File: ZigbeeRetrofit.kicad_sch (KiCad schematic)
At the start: 23 parts, among them J1 110990030, J2 U.FL-R-SMT-1(10), J3 TC2050-IDC-NL, U1 CC2531F256RHAT, U2 SPX3819M5-L-3-3, Y1 32 Mhz, Y2 32.768 khz

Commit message: Updated crystals
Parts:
- removed Y2: 32.768 khz, symbol Device:Crystal
- added Y2: ECS-.327-12.5-34RR-TR, ECS-.327-12:XTAL_ECS-.327-12.5-34RR-TR, symbol ECS-.327-12.5-34RR-TR:ECS-.327-12.5-34RR-TR
- Y1: footprint XTAL_ECS-320-13-42-CKM-TR -> ECS-320-13-42-CKM-TR:XTAL_ECS-320-13-42-CKM-TR
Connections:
- net GND: now also Y1.2 (GND), Y1.4 (GND)
- net at C11.1, U1.32 (P2_4/XOSC32K_Q1): now also Y2.1
- net at C12.1, U1.33 (P2_3/XOSC32K_Q2): now also Y2.2
- no-connect marks 28 -> 27
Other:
- moved on the sheet: C12, C4, C7

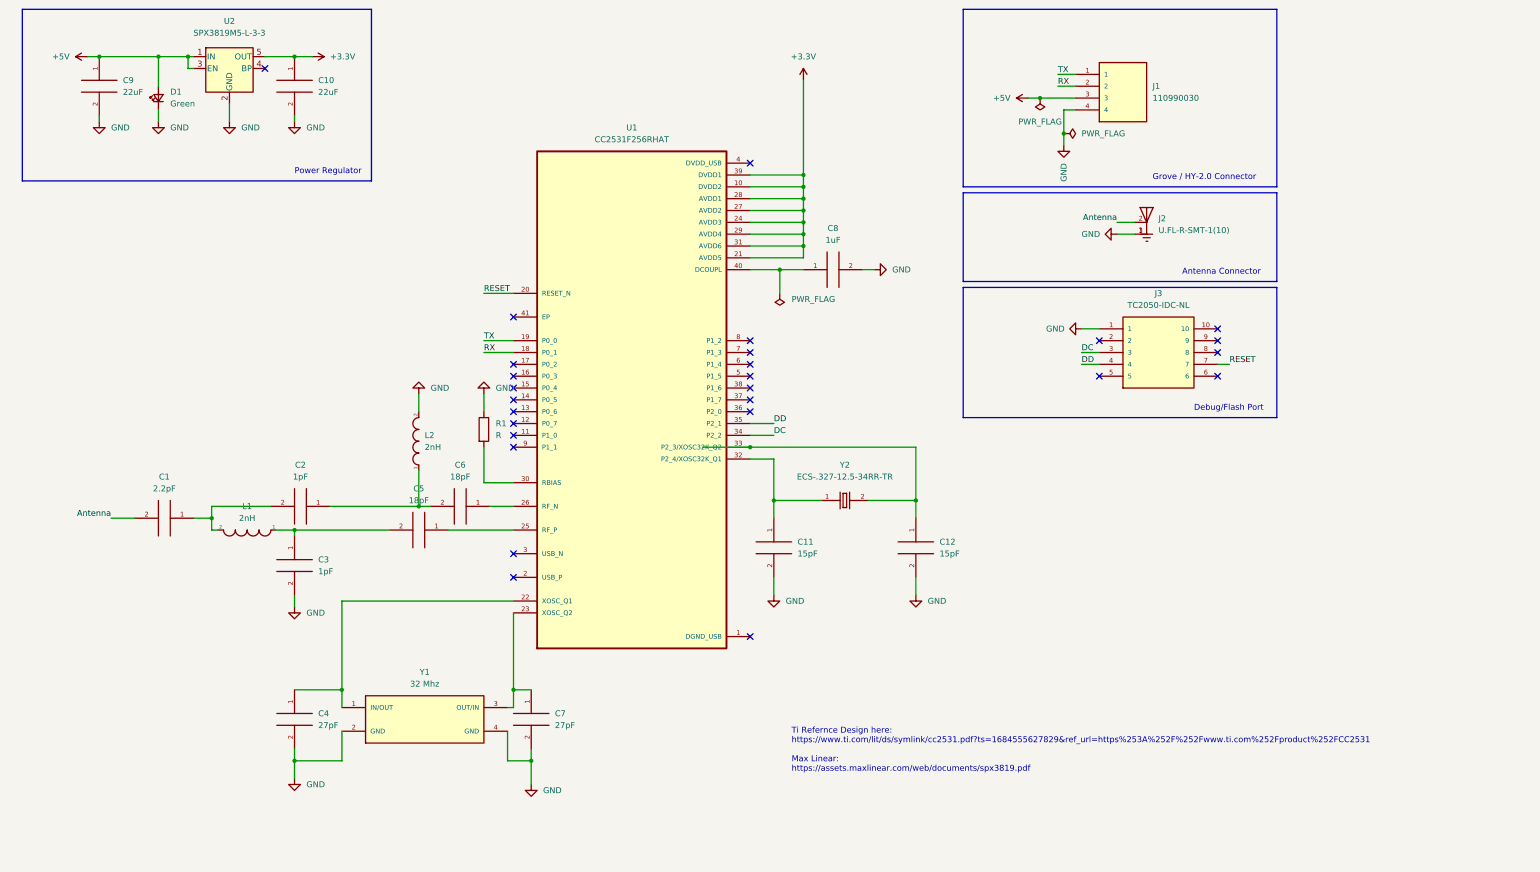
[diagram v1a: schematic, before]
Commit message: Updated Symbols to clear ERC
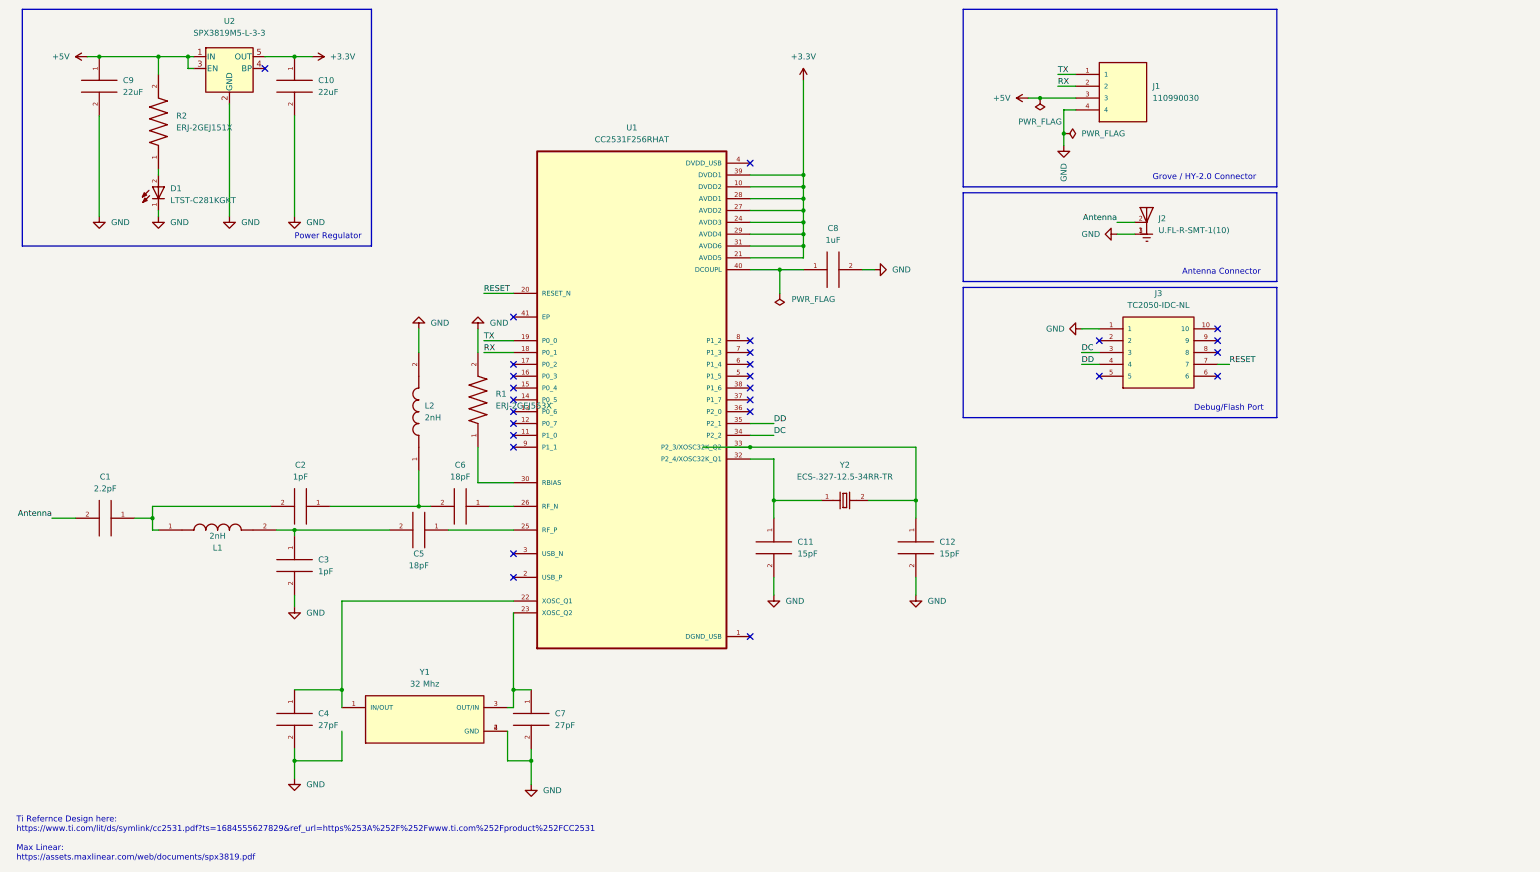
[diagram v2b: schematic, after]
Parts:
- removed D1: Green, symbol Device:LED_Small
- removed L1, L2: 2nH, symbol pspice:INDUCTOR
- removed R1: R, Resistor_SMD:R_0402_1005Metric, symbol Device:R
- added D1: LTST-C281KGKT, LTST-C281KGKT:0402(POL), symbol LTST-C281KGKT:LTST-C281KGKT
- added L1, L2: 2nH, MHQ1005P2N0ST000:INDC1006X60N, symbol MHQ1005P2N0ST000:MHQ1005P2N0ST000
- added R1: ERJ-2GEJ563X, ERJ-2GEJ563X:RES_ERJ-2GEJ563X, symbol ERJ-2GEJ563X:ERJ-2GEJ563X
- added R2: ERJ-2GEJ151X, ERJ-2GEJ151X:RES_ERJ-2GEJ151X, symbol ERJ-2GEJ151X:ERJ-2GEJ151X
- J3: Availability (none) -> In Stock; Check_prices (none) -> https://www.snapeda.com/parts/TC2050-IDC-NL/Tag-Connect+LLC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; MF (none) -> Tag-Connect LLC; MP (none) -> TC2050-IDC-NL; Package (none) -> None; Price (none) -> None; Purchase-URL (none) -> https://pricing.snapeda.com/search?q=TC2050-IDC-NL&ref=eda; SnapEDA_Link (none) -> https://www.snapeda.com/parts/TC2050-IDC-NL/Tag-Connect+LLC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
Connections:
- net +5V: now also R2.2
- net GND: now also D1.1, L2.2, R1.2
- net at C1.1, C2.2: now also L1.1
- net at C3.1, C5.2: now also L1.2
- net at C2.1, C6.2: now also L2.1
- net at U1.30 (RBIAS): now also R1.1
- new net: D1.2, R2.1
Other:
- moved on the sheet: C1

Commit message: Updated layout with 3d models
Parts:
- J1: value 110990030 -> 114020164
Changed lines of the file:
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@@
       (effects (font (size 1.27 1.27)) (justify left))
     )
-    (property "Value" "110990030" (id 1) (at 256.54 33.0199 0)
+    (property "Value" "114020164" (id 1) (at 256.54 33.0199 0)
       (effects (font (size 1.27 1.27)) (justify left))
     )
@@
     )
     (path "/8e4e635d-33a0-4932-856a-6a690a34c395"
-      (reference "J1") (unit 1) (value "110990030") (footprint "110990030:SEEED_110990030")
+      (reference "J1") (unit 1) (value "114020164") (footprint "110990030:SEEED_110990030")
     )
     (path "/33aac899-fc0a-4e6d-a4e5-d2f7cbb5983c"

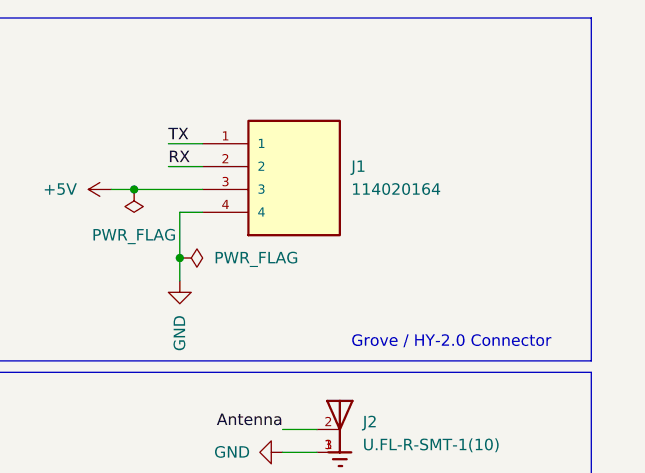
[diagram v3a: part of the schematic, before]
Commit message: Added ground
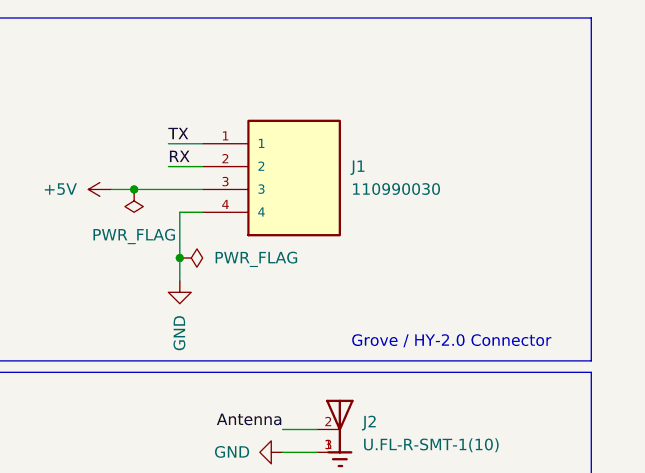
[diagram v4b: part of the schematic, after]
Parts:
- J1: value 114020164 -> 110990030; Availability (none) -> In Stock; Check_prices (none) -> https://www.snapeda.com/parts/114020164/Seeed+Technology+Co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; MF (none) -> Seeed Technology Co., Ltd; MP (none) -> 114020164; Package (none) -> None; Price (none) -> None; Purchase-URL (none) -> https://www.snapeda.com/api/url_track_click_mouser/?unipart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; SnapEDA_Link (none) -> https://www.snapeda.com/parts/114020164/Seeed+Technology+Co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
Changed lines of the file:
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@@
       (effects (font (size 1.27 1.27)) (justify left))
     )
-    (property "Value" "114020164" (id 1) (at 256.54 33.0199 0)
+    (property "Value" "110990030" (id 1) (at 256.54 33.0199 0)
       (effects (font (size 1.27 1.27)) (justify left))
     )
@@
     )
     (property "STANDARD" "Manufacturer Recommendations" (id 7) (at 250.19 30.48 0)
+      (effects (font (size 1.27 1.27)) (justify bottom) hide)
+    )
+    (property "MF" "Seeed Technology Co., Ltd" (id 8) (at 250.19 30.48 0)
+      (effects (font (size 1.27 1.27)) (justify bottom) hide)
+    )
+    (property "Package" "None" (id 9) (at 250.19 30.48 0)
+      (effects (font (size 1.27 1.27)) (justify bottom) hide)
+    )
+    (property "Price" "None" (id 10) (at 250.19 30.48 0)
+      (effects (font (size 1.27 1.27)) (justify bottom) hide)
+    )
+    (property "Check_prices" "https://www.snapeda.com/parts/114020164/Seeed+Technology+Co.%252C+Ltd/view-part/?ref=eda" (id 11) (at 250.19 30.48 0)
+      (effects (font (size 1.27 1.27)) (justify bottom) hide)
+    )
+    (property "SnapEDA_Link" "https://www.snapeda.com/parts/114020164/Seeed+Technology+Co.%252C+Ltd/view-part/?ref=snap" (id 12) (at 250.19 30.48 0)
+      (effects (font (size 1.27 1.27)) (justify bottom) hide)
+    )
+    (property "MP" "114020164" (id 13) (at 250.19 30.48 0)
+      (effects (font (size 1.27 1.27)) (justify bottom) hide)
+    )
+    (property "Purchase-URL" "https://www.snapeda.com/api/url_track_click_mouser/?unipart_id=5310052&manufacturer=Seeed Technology Co., Ltd&part_name=114020164&search_term=None" (id 14) (at 250.19 30.48 0)
+      (effects (font (size 1.27 1.27)) (justify bottom) hide)
+    )
+    (property "Description" "\nGROVE FEMALE HEADER R/A 20PACK\n" (id 15) (at 250.19 30.48 0)
+      (effects (font (size 1.27 1.27)) (justify bottom) hide)
+    )
+    (property "Availability" "In Stock" (id 16) (at 250.19 30.48 0)
       (effects (font (size 1.27 1.27)) (justify bottom) hide)
     )
@@
     )
     (path "/8e4e635d-33a0-4932-856a-6a690a34c395"
-      (reference "J1") (unit 1) (value "114020164") (footprint "110990030:SEEED_110990030")
+      (reference "J1") (unit 1) (value "110990030") (footprint "110990030:SEEED_110990030")
     )
     (path "/33aac899-fc0a-4e6d-a4e5-d2f7cbb5983c"

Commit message: Updated grove connector
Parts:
- J1: value 110990030 -> 110990037; footprint 110990030:SEEED_110990030 -> Connector_JST:JST_PH_S4B-PH-K_1x04_P2.00mm_Horizontal; symbol 110990030:110990030 -> Connector:Conn_01x04_Male; Check_prices https://www.snapeda.com/parts/114020164/Seeed+Technology+Co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 -> (none); MP 114020164 -> 110990037; Purchase-URL https://www.snapeda.com/api/url_track_click_mouser/?unipart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 -> (none); SnapEDA_Link https://www.snapeda.com/parts/114020164/Seeed+Technology+Co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 -> (none)

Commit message: Revision 0.2 - Draft
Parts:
- U1: footprint CC2531F256RHAT:QFN50P600X600X100-41N -> QFN50P600X600X100-41N
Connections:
- net +3.3V: now also J3.2, J3.9
- net GND: now also U1.41 (EP)
- no-connect marks 27 -> 24
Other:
- moved on the sheet: C6, R1

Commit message: Revision 0.2 - Final
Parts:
- R1: value ERJ-2GEJ563X -> 56K Ohm
- R2: value ERJ-2GEJ151X -> 150 Ohm
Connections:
- net +5V: now also J1.2 (Pin_2); no longer J1.3 (Pin_3)
- net GND: now also J1.1 (Pin_1); no longer J1.4 (Pin_4)
- net RX: now also J1.3 (Pin_3); no longer J1.2 (Pin_2)
- net TX: now also J1.4 (Pin_4); no longer J1.1 (Pin_1)
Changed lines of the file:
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@@
   (title_block
     (title "ZigbeeRetrofit")
-    (date "2023-08-13")
-    (rev "0.1")
+    (date "2023-10-14")
+    (rev "0.2")
     (comment 1 "Drawn by: Timothy Finday")
     (comment 2 "Target Package: 0402")
@@
   (junction (at 181.61 59.69) (diameter 0) (color 0 0 0 0)
   )
-  (junction (at 236.22 30.48) (diameter 0) (color 0 0 0 0)
-  )
   (junction (at 181.61 62.23) (diameter 0) (color 0 0 0 0)
   )
+  (junction (at 236.22 35.56) (diameter 0) (color 0 0 0 0)
+  )
   (junction (at 181.61 52.07) (diameter 0) (color 0 0 0 0)
   )
@@
   (junction (at 123.19 175.26) (diameter 0) (color 0 0 0 0)
   )
+  (junction (at 236.22 33.02) (diameter 0) (color 0 0 0 0)
+  )
   (junction (at 30.48 24.13) (diameter 0) (color 0 0 0 0)
   )
@@
   )
   (junction (at 176.53 69.85) (diameter 0) (color 0 0 0 0)
-  )
-  (junction (at 236.22 27.94) (diameter 0) (color 0 0 0 0)
   )
   (junction (at 72.39 175.26) (diameter 0) (color 0 0 0 0)
@@
     (stroke (width 0) (type default) (color 0 0 0 0))
   )
+  (wire (pts (xy 241.3 27.94) (xy 246.38 27.94))
+    (stroke (width 0) (type default) (color 0 0 0 0))
+  )
   (wire (pts (xy 43.18 24.13) (xy 49.53 24.13))
     (stroke (width 0) (type default) (color 0 0 0 0))
@@
     (stroke (width 0) (type default) (color 0 0 0 0))
   )
+  (wire (pts (xy 236.22 35.56) (xy 246.38 35.56))
+    (stroke (width 0) (type default) (color 0 0 0 0))
+  )
   (wire (pts (xy 99.06 113.03) (xy 99.06 120.65))
     (stroke (width 0) (type default) (color 0 0 0 0))
@@
     (stroke (width 0) (type default) (color 0 0 0 0))
   )
-  (wire (pts (xy 233.68 30.48) (xy 236.22 30.48))
-    (stroke (width 0) (type default) (color 0 0 0 0))
-  )
   (wire (pts (xy 113.03 74.93) (xy 119.38 74.93))
     (stroke (width 0) (type default) (color 0 0 0 0))
@@
     (stroke (width 0) (type default) (color 0 0 0 0))
   )
+  (wire (pts (xy 241.3 30.48) (xy 246.38 30.48))
+    (stroke (width 0) (type default) (color 0 0 0 0))
+  )
   (wire (pts (xy 72.39 125.73) (xy 72.39 127))
     (stroke (width 0) (type default) (color 0 0 0 0))
@@
     (stroke (width 0) (type default) (color 0 0 0 0))
   )
-  (wire (pts (xy 242.57 33.02) (xy 246.38 33.02))
-    (stroke (width 0) (type default) (color 0 0 0 0))
-  )
   (wire (pts (xy 68.58 125.73) (xy 72.39 125.73))
     (stroke (width 0) (type default) (color 0 0 0 0))
@@
     (stroke (width 0) (type default) (color 0 0 0 0))
   )
+  (wire (pts (xy 233.68 33.02) (xy 236.22 33.02))
+    (stroke (width 0) (type default) (color 0 0 0 0))
+  )
   (wire (pts (xy 181.61 54.61) (xy 181.61 52.07))
     (stroke (width 0) (type default) (color 0 0 0 0))
@@
     (stroke (width 0) (type default) (color 0 0 0 0))
   )
-  (wire (pts (xy 242.57 35.56) (xy 246.38 35.56))
-    (stroke (width 0) (type default) (color 0 0 0 0))
-  )
   (wire (pts (xy 119.38 80.01) (xy 110.49 80.01))
     (stroke (width 0) (type default) (color 0 0 0 0))
@@
     (stroke (width 0) (type default) (color 0 0 0 0))
   )
-  (wire (pts (xy 236.22 27.94) (xy 246.38 27.94))
-    (stroke (width 0) (type default) (color 0 0 0 0))
-  )
   (wire (pts (xy 72.39 172.72) (xy 72.39 175.26))
     (stroke (width 0) (type default) (color 0 0 0 0))
@@
     (stroke (width 0) (type default) (color 0 0 0 0))
   )
-  (wire (pts (xy 236.22 30.48) (xy 246.38 30.48))
-    (stroke (width 0) (type default) (color 0 0 0 0))
-  )
   (wire (pts (xy 175.26 119.38) (xy 185.42 119.38))
     (stroke (width 0) (type default) (color 0 0 0 0))
@@
     (stroke (width 0) (type default) (color 0 0 0 0))
   )
+  (wire (pts (xy 236.22 27.94) (xy 236.22 33.02))
+    (stroke (width 0) (type default) (color 0 0 0 0))
+  )
   (wire (pts (xy 170.18 107.95) (xy 205.74 107.95))
     (stroke (width 0) (type default) (color 0 0 0 0))
@@
     (stroke (width 0) (type default) (color 0 0 0 0))
   )
+  (wire (pts (xy 236.22 33.02) (xy 246.38 33.02))
+    (stroke (width 0) (type default) (color 0 0 0 0))
+  )
   (polyline (pts (xy 88.9 13.97) (xy 13.97 13.97))
     (stroke (width 0) (type default) (color 0 0 0 0))
@@
     (stroke (width 0) (type default) (color 0 0 0 0))
   )
-  (wire (pts (xy 233.68 27.94) (xy 236.22 27.94))
+  (wire (pts (xy 233.68 35.56) (xy 236.22 35.56))
     (stroke (width 0) (type default) (color 0 0 0 0))
   )
@@
     (effects (font (size 1.27 1.27)) (justify left bottom))
   )
-  (label "TX" (at 242.57 35.56 0)
+  (label "TX" (at 241.3 27.94 0)
     (effects (font (size 1.27 1.27)) (justify left bottom))
   )
@@
     (effects (font (size 1.27 1.27)) (justify left bottom))
   )
-  (label "RX" (at 242.57 33.02 0)
+  (label "RX" (at 241.3 30.48 0)
     (effects (font (size 1.27 1.27)) (justify left bottom))
   )
@@
     (pin "2")
   )
-  (symbol (lib_id "power:GND") (at 233.68 27.94 270) (unit 1)
+  (symbol (lib_id "power:GND") (at 233.68 35.56 270) (unit 1)
     (in_bom yes) (on_board yes)
-    (property "Reference" "#PWR0105" (id 0) (at 227.33 27.94 0)
-      (effects (font (size 1.27 1.27)) hide)
-    )
-    (property "Value" "GND" (id 1) (at 229.87 27.9401 90)
+    (property "Reference" "#PWR0105" (id 0) (at 227.33 35.56 0)
+      (effects (font (size 1.27 1.27)) hide)
+    )
+    (property "Value" "GND" (id 1) (at 229.87 35.5601 90)
       (effects (font (size 1.27 1.27)) (justify right))
     )
-    (property "Footprint" "" (id 2) (at 233.68 27.94 0)
-      (effects (font (size 1.27 1.27)) hide)
-    )
-    (property "Datasheet" "" (id 3) (at 233.68 27.94 0)
+    (property "Footprint" "" (id 2) (at 233.68 35.56 0)
+      (effects (font (size 1.27 1.27)) hide)
+    )
+    (property "Datasheet" "" (id 3) (at 233.68 35.56 0)
       (effects (font (size 1.27 1.27)) hide)
     )
@@
       (effects (font (size 1.27 1.27)) (justify right))
     )
-    (property "Value" "ERJ-2GEJ151X" (id 1) (at 46.99 39.3699 90)
+    (property "Value" "150 Ohm" (id 1) (at 46.99 39.3699 90)
       (effects (font (size 1.27 1.27)) (justify right))
     )
@@
       (effects (font (size 1.27 1.27)) (justify bottom) hide)
     )
-    (property "Description" "\nResistor Thick Film 0402 150 Ohm 5% 1/10 Watt ±200ppm °C Surface Mount Punched Carrier Tape and Reel\n" (id 14) (at 43.18 38.1 0)
+    (property "Description" "Resistor Thick Film 0402 150 Ohm 5% 1/10 Watt ±200ppm °C Surface Mount Punched Carrier Tape and Reel" (id 14) (at 43.18 38.1 0)
       (effects (font (size 1.27 1.27)) (justify bottom) hide)
     )
@@
       (effects (font (size 1.27 1.27)) (justify right))
     )
-    (property "Value" "ERJ-2GEJ563X" (id 1) (at 113.03 99.0599 90)
+    (property "Value" "56K Ohm" (id 1) (at 113.03 99.0599 90)
       (effects (font (size 1.27 1.27)) (justify right))
     )
@@
       (effects (font (size 1.27 1.27)) (justify bottom) hide)
     )
-    (property "Description" "\nRes Thick Film 1.0 x 0.5 mm 56K Ohm 5% 0.1W(1/10W) 200ppm/ C Molded SMD Punched Carrier T/R\n" (id 14) (at 109.22 97.79 0)
+    (property "Description" "Res Thick Film 1.0 x 0.5 mm 56K Ohm 5% 0.1W(1/10W) 200ppm/ C Molded SMD Punched Carrier T/R" (id 14) (at 109.22 97.79 0)
       (effects (font (size 1.27 1.27)) (justify bottom) hide)
     )
@@
     (pin "1")
   )
-  (symbol (lib_id "power:+5V") (at 233.68 30.48 90) (unit 1)
+  (symbol (lib_id "power:+5V") (at 233.68 33.02 90) (unit 1)
     (in_bom yes) (on_board yes)
-    (property "Reference" "#PWR08" (id 0) (at 237.49 30.48 0)
-      (effects (font (size 1.27 1.27)) hide)
-    )
-    (property "Value" "+5V" (id 1) (at 229.87 30.4799 90)
-      (effects (font (size 1.27 1.27)) (justify left))
-    )
-    (property "Footprint" "" (id 2) (at 233.68 30.48 0)
-      (effects (font (size 1.27 1.27)) hide)
-    )
-    (property "Datasheet" "" (id 3) (at 233.68 30.48 0)
+    (property "Reference" "#PWR08" (id 0) (at 237.49 33.02 0)
+      (effects (font (size 1.27 1.27)) hide)
+    )
+    (property "Value" "+5V" (id 1) (at 229.87 33.0199 90)
+      (effects (font (size 1.27 1.27)) (justify left))
+    )
+    (property "Footprint" "" (id 2) (at 233.68 33.02 0)
+      (effects (font (size 1.27 1.27)) hide)
+    )
+    (property "Datasheet" "" (id 3) (at 233.68 33.02 0)
       (effects (font (size 1.27 1.27)) hide)
     )
@@
     (pin "9")
   )
-  (symbol (lib_id "power:PWR_FLAG") (at 236.22 30.48 180) (unit 1)
+  (symbol (lib_id "power:PWR_FLAG") (at 236.22 35.56 180) (unit 1)
     (in_bom yes) (on_board yes)
-    (property "Reference" "#FLG01" (id 0) (at 236.22 32.385 0)
-      (effects (font (size 1.27 1.27)) hide)
-    )
-    (property "Value" "PWR_FLAG" (id 1) (at 236.22 34.29 0))
-    (property "Footprint" "" (id 2) (at 236.22 30.48 0)
-      (effects (font (size 1.27 1.27)) hide)
-    )
-    (property "Datasheet" "~" (id 3) (at 236.22 30.48 0)
+    (property "Reference" "#FLG01" (id 0) (at 236.22 37.465 0)
+      (effects (font (size 1.27 1.27)) hide)
+    )
+    (property "Value" "PWR_FLAG" (id 1) (at 236.22 39.37 0))
+    (property "Footprint" "" (id 2) (at 236.22 35.56 0)
+      (effects (font (size 1.27 1.27)) hide)
+    )
+    (property "Datasheet" "~" (id 3) (at 236.22 35.56 0)
       (effects (font (size 1.27 1.27)) hide)
     )
@@
     )
     (path "/5a62ce53-a054-4039-998b-7d9bce925e58"
-      (reference "R1") (unit 1) (value "ERJ-2GEJ563X") (footprint "ERJ-2GEJ563X:RES_ERJ-2GEJ563X")
+      (reference "R1") (unit 1) (value "56K Ohm") (footprint "ERJ-2GEJ563X:RES_ERJ-2GEJ563X")
     )
     (path "/4220d684-6877-4df8-9197-96ae3e159004"
-      (reference "R2") (unit 1) (value "ERJ-2GEJ151X") (footprint "ERJ-2GEJ151X:RES_ERJ-2GEJ151X")
+      (reference "R2") (unit 1) (value "150 Ohm") (footprint "ERJ-2GEJ151X:RES_ERJ-2GEJ151X")
     )
     (path "/afcc2660-b661-41d1-94b1-2004648048f1"
